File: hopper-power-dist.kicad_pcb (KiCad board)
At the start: 2 copper layers, 109 x 79 mm, 29 parts, among them J1 XT60PW-M, J2 XT60PW-M, J3 B2B-XH-A(LF)(SN), J4 B2B-XH-A(LF)(SN), J5 XT60-F, J6 XT60PW-F, J7 XT60PW-F, J8 XT60PW-F, J9 XT60PW-F, SW1 FT_Power_Switch

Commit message: Further tweaks to v2 design
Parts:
- added C3: 4.7μF, Capacitor_SMD:C_0805_2012Metric, F.Cu at (140.0, 81.0)
- added C4: 1000pF, Capacitor_SMD:C_1206_3216Metric, F.Cu at (140.0, 66.5)
- added C5: 1000pF, Capacitor_SMD:C_1206_3216Metric, F.Cu at (81.0, 78.0)
- added C6: 470pF, Capacitor_SMD:C_1206_3216Metric, F.Cu at (140.0, 76.0)
- added L1: 12μF, SamacSys_Parts:LPS6235123MRC, F.Cu at (147.0, 68.5)
- added L2: 12μF, SamacSys_Parts:LPS6235123MRC, F.Cu at (144.5, 88.0)
- C2: value 220μF -> 4.7μF; footprint benbokser:CP_Elec_8x10_150CRZ -> SamacSys_Parts:CAPC3225X270N
- moved C2 64.5 mm to (146.5, 80.5), turned to -90 degrees
- moved J5 21.4 mm to (154.5, 110.5)
- moved H2 13.0 mm to (129.0, 106.5)
- moved H1 11.5 mm to (129.0, 119.5)
- moved D3 10.0 mm to (118.5, 104.5)
- moved R2 10.0 mm to (118.5, 107.0)
- moved F1 9.06 mm to (147.5, 76.0)
- moved S1 6.40 mm to (146.0, 99.0), turned to 90 degrees
- moved J4 3.61 mm to (80.0, 85.5), turned to 90 degrees
- moved PS1 3.50 mm to (133.9, 70.4)
- moved D2 3.20 mm to (79.5, 70.0), turned to -90 degrees
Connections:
- C2 pad 2: Net-(C2-Pad2) -> GND
- D2 pad 1: Net-(C2-Pad1) -> /+12V
- D2 pad 2: Net-(C2-Pad2) -> /-12V
- F1 pad 2: Net-(C1-Pad1) -> Net-(C2-Pad1)
- J4 pad 1: Net-(C2-Pad1) -> /+12V
- J4 pad 2: Net-(C2-Pad2) -> /-12V
- PS1 pad 1: Net-(C1-Pad1) -> Net-(PS1-Pad1)
- PS1 pad 2: GND -> Net-(PS1-Pad2)
- PS1 pad 4: Net-(C2-Pad1) -> /+12V
- PS1 pad 5: Net-(C2-Pad2) -> /-12V
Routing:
- net Net-(J1-Pad1): track 90.0 -> 0.00 mm
- net /+12V: track 0.00 -> 53.0 mm
- net GND: track 1.93 -> 31.0 mm
- net Net-(PS1-Pad1): track 0.00 -> 28.9 mm
- net Net-(J2-Pad1): track 58.5 -> 32.4 mm
- net /-12V: track 0.00 -> 25.5 mm, vias 0 -> 1
- net Net-(PS1-Pad3): track 0.00 -> 18.9 mm
- net Net-(PS1-Pad2): track 0.00 -> 17.1 mm
- net Net-(H1-Pad1): track 14.3 -> 0.14 mm
- net Net-(C2-Pad1): track 0.00 -> 12.0 mm
- net /HS: track 0.00 -> 0.85 mm
- added copper zone on F.Cu, net /+12V
- added copper zone on B.Cu, net /-12V
- added copper zone on B.Cu, net Net-(H1-Pad1)
- added copper zone on F.Cu, net Net-(H1-Pad1)
- added copper zone on B.Cu, net Net-(J1-Pad1)
- added copper zone on F.Cu, net Net-(J1-Pad1)
- added copper zone on B.Cu, net Net-(J2-Pad1)
- added copper zone on F.Cu, net Net-(J2-Pad1)
- removed copper zone on F.Cu, net Net-(C2-Pad1)
- removed copper zone on B.Cu, net Net-(C2-Pad2)
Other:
- board text added: "Bokser hopper-power-dist rev02 08-23-22 REx Lab"
- board text removed: "Bokser hopper-power-dist rev02 08-22-22 REx Lab"

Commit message: Minor improvements made
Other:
- board text added: "Bokser hopper-power-dist rev02 08-28-22 REx Lab"
- board text removed: "Bokser hopper-power-dist rev02 08-23-22 REx Lab"
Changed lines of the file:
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@@
   )
   (gr_rect locked (start 55 63) (end 164 142) (layer "Edge.Cuts") (width 0.2) (fill none))
-  (gr_text "Bokser\nhopper-power-dist rev02\n08-23-22\nREx Lab\n" (at 102.5 100.5) (layer "F.SilkS")
+  (gr_text "Bokser\nhopper-power-dist rev02\n08-28-22\nREx Lab\n" (at 102.5 100.5) (layer "F.SilkS")
     (effects (font (size 1.2 1.2) (thickness 0.3) italic) (justify left))
   )
   (segment (start 153.15 76) (end 153.75 75.4) (width 0.25) (layer "F.Cu") (net 1))
+  (segment (start 153.5 82.5) (end 153.65 82.5) (width 1) (layer "F.Cu") (net 2))
+  (segment (start 153.65 82.5) (end 153.75 82.6) (width 1) (layer "F.Cu") (net 2))
+  (segment (start 152.85 81.85) (end 153.5 82.5) (width 1) (layer "F.Cu") (net 2))
   (segment (start 146.5 81.85) (end 146.5 87.85) (width 1) (layer "F.Cu") (net 2))
-  (segment (start 146.5 81.85) (end 153 81.85) (width 1) (layer "F.Cu") (net 2))
-  (segment (start 153 81.85) (end 153.75 82.6) (width 0.25) (layer "F.Cu") (net 2))
   (segment (start 146.5 87.85) (end 146.65 88) (width 0.25) (layer "F.Cu") (net 2))
-  (segment (start 67.85 78) (end 65.25 75.4) (width 0.25) (layer "F.Cu") (net 2))
+  (segment (start 146.5 81.85) (end 152.85 81.85) (width 1) (layer "F.Cu") (net 2))
+  (segment (start 67.85 78) (end 65.25 75.4) (width 1) (layer "F.Cu") (net 2))
   (segment (start 115.5875 104.5) (end 117.5125 104.5) (width 0.25) (layer "F.Cu") (net 2))
-  (segment (start 79.525 78) (end 67.85 78) (width 0.25) (layer "F.Cu") (net 2))
+  (segment (start 79.525 78) (end 67.85 78) (width 1) (layer "F.Cu") (net 2))
   (via (at 115.5875 104.5) (size 0.8) (drill 0.4) (layers "F.Cu" "B.Cu") (free) (net 2))
   (segment (start 119.4125 104.625) (end 119.2875 104.5) (width 0.25) (layer "F.Cu") (net 3))
@@
   (segment (start 146.215 75.285) (end 149.15 72.35) (width 1) (layer "F.Cu") (net 14))
   (segment (start 146.215 76) (end 146.215 75.285) (width 1) (layer "F.Cu") (net 14))
-  (segment (start 146.215 76) (end 146.215 78.865) (width 0.25) (layer "F.Cu") (net 14))
+  (segment (start 146.215 76) (end 146.215 78.865) (width 1) (layer "F.Cu") (net 14))
   (segment (start 136.5425 99) (end 133.86 96.3175) (width 0.25) (layer "F.Cu") (net 17))
   (segment (start 140.92 99) (end 136.5425 99) (width 0.25) (layer "F.Cu") (net 17))
@@
   (segment (start 140 67.975) (end 140 68) (width 0.25) (layer "F.Cu") (net 19))
   (segment (start 133.86 70.38) (end 141.12 70.38) (width 1) (layer "F.Cu") (net 19))
-  (segment (start 140 68) (end 141.5 69.5) (width 0.25) (layer "F.Cu") (net 19))
-  (segment (start 140 77.475) (end 140 80.05) (width 0.25) (layer "F.Cu") (net 19))
-  (segment (start 143 72.85) (end 143 76.5) (width 0.25) (layer "F.Cu") (net 19))
-  (segment (start 142.025 77.475) (end 140 77.475) (width 0.25) (layer "F.Cu") (net 19))
+  (segment (start 140 68) (end 141.5 69.5) (width 1) (layer "F.Cu") (net 19))
+  (segment (start 140 77.475) (end 140 80.05) (width 1) (layer "F.Cu") (net 19))
+  (segment (start 143 72.85) (end 143 76.5) (width 1) (layer "F.Cu") (net 19))
+  (segment (start 142.025 77.475) (end 140 77.475) (width 1) (layer "F.Cu") (net 19))
   (segment (start 143 68.5) (end 145 68.5) (width 1) (layer "F.Cu") (net 19))
-  (segment (start 143 76.5) (end 142.025 77.475) (width 0.25) (layer "F.Cu") (net 19))
-  (segment (start 145 70.85) (end 143 72.85) (width 0.25) (layer "F.Cu") (net 19))
-  (segment (start 145 68.5) (end 145 70.85) (width 0.25) (layer "F.Cu") (net 19))
+  (segment (start 143 76.5) (end 142.025 77.475) (width 1) (layer "F.Cu") (net 19))
+  (segment (start 145 70.85) (end 143 72.85) (width 1) (layer "F.Cu") (net 19))
+  (segment (start 145 68.5) (end 145 70.85) (width 1) (layer "F.Cu") (net 19))
   (segment (start 142.5 84) (end 140.45 81.95) (width 1) (layer "F.Cu") (net 20))
   (segment (start 140.45 81.95) (end 140 81.95) (width 1) (layer "F.Cu") (net 20))
@@
   (segment (start 142.5 87.85) (end 142.5 84) (width 1) (layer "F.Cu") (net 20))
   (segment (start 79.5 75) (end 82.5 78) (width 1) (layer "F.Cu") (net 21))
-  (segment (start 140 74.525) (end 138.475 73) (width 0.25) (layer "F.Cu") (net 21))
+  (segment (start 140 74.525) (end 138.475 73) (width 1) (layer "F.Cu") (net 21))
   (segment (start 82.5 78) (end 88.14 78) (width 1) (layer "F.Cu") (net 21))
-  (segment (start 138.475 73) (end 126.5 73) (width 0.25) (layer "F.Cu") (net 21))
+  (segment (start 138.475 73) (end 126.5 73) (width 1) (layer "F.Cu") (net 21))
   (segment (start 79.5 73.5) (end 79.5 75) (width 1) (layer "F.Cu") (net 21))
-  (via (at 126.5 73) (size 0.8) (drill 0.4) (layers "F.Cu" "B.Cu") (net 21))
-  (segment (start 137.5 66) (end 126 66) (width 0.25) (layer "F.Cu") (net 22))
-  (segment (start 140 65.025) (end 138.475 65.025) (width 0.25) (layer "F.Cu") (net 22))
-  (segment (start 138.475 65.025) (end 137.5 66) (width 0.25) (layer "F.Cu") (net 22))
-  (segment (start 124.16 67.84) (end 88.14 67.84) (width 0.25) (layer "F.Cu") (net 22))
-  (segment (start 126 66) (end 124.16 67.84) (width 0.25) (layer "F.Cu") (net 22))
+  (via (at 126.5 73) (size 2) (drill 1) (layers "F.Cu" "B.Cu") (net 21))
+  (segment (start 137.5 66) (end 126 66) (width 1) (layer "F.Cu") (net 22))
+  (segment (start 140 65.025) (end 138.475 65.025) (width 1) (layer "F.Cu") (net 22))
+  (segment (start 138.475 65.025) (end 137.5 66) (width 1) (layer "F.Cu") (net 22))
+  (segment (start 124.16 67.84) (end 88.14 67.84) (width 1) (layer "F.Cu") (net 22))
+  (segment (start 126 66) (end 124.16 67.84) (width 1) (layer "F.Cu") (net 22))
   (zone (net 4) (net_name "Net-(J1-Pad1)") (layers F&B.Cu) (hatch edge 0.508)
     (connect_pads (clearance 0.508))

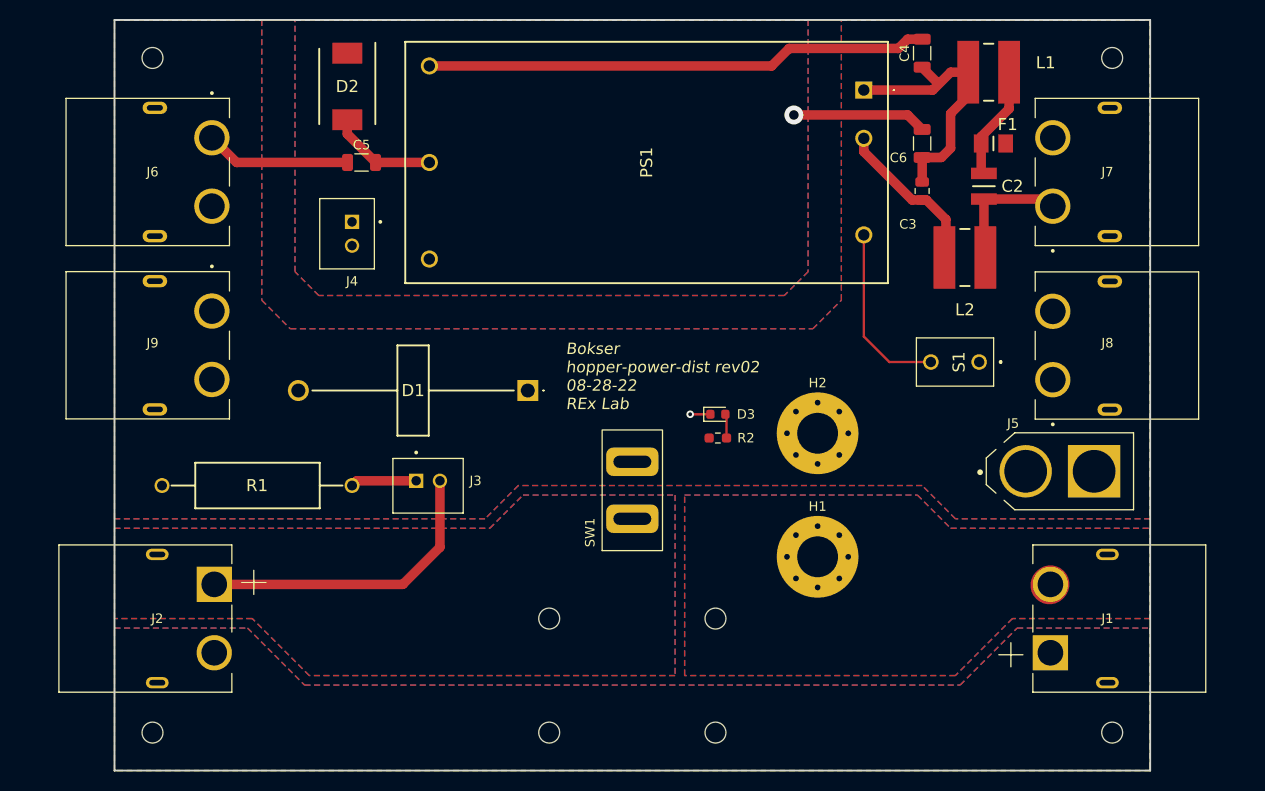
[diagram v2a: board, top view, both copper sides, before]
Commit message: Added spark suppression and changed thermal reliefs to solid on high power pads
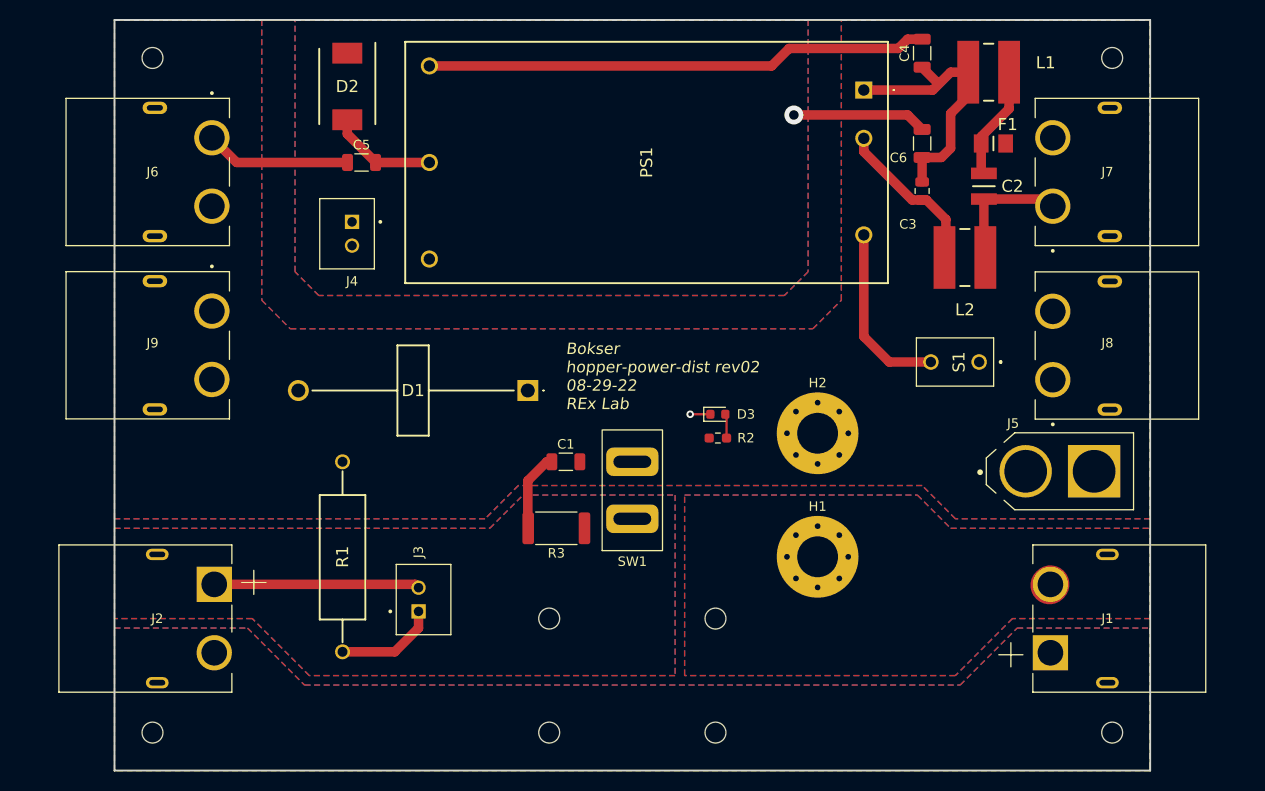
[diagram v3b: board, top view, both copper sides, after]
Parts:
- added C1: 0.22μF, Capacitor_SMD:C_1206_3216Metric, F.Cu at (102.5, 109.5)
- added R3: 290Ω, Resistor_SMD:R_2512_6332Metric, F.Cu at (101.5, 116.5)
- R1: value 365Ω -> 360Ω
- moved R1 17.5 mm to (79.0, 129.5), turned to 90 degrees
- moved J3 12.5 mm to (87.0, 124.0), turned to -90 degrees
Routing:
- net Net-(J2-Pad1): track 32.4 -> 21.6 mm
- net Net-(C1-Pad1): track 0.00 -> 8.37 mm
- net Net-(J3-Pad1): track 6.96 -> 10.8 mm
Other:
- board text added: "Bokser hopper-power-dist rev02 08-29-22 REx Lab"
- board text removed: "Bokser hopper-power-dist rev02 08-28-22 REx Lab"
